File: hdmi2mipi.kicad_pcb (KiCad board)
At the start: 2 copper layers, 1 part

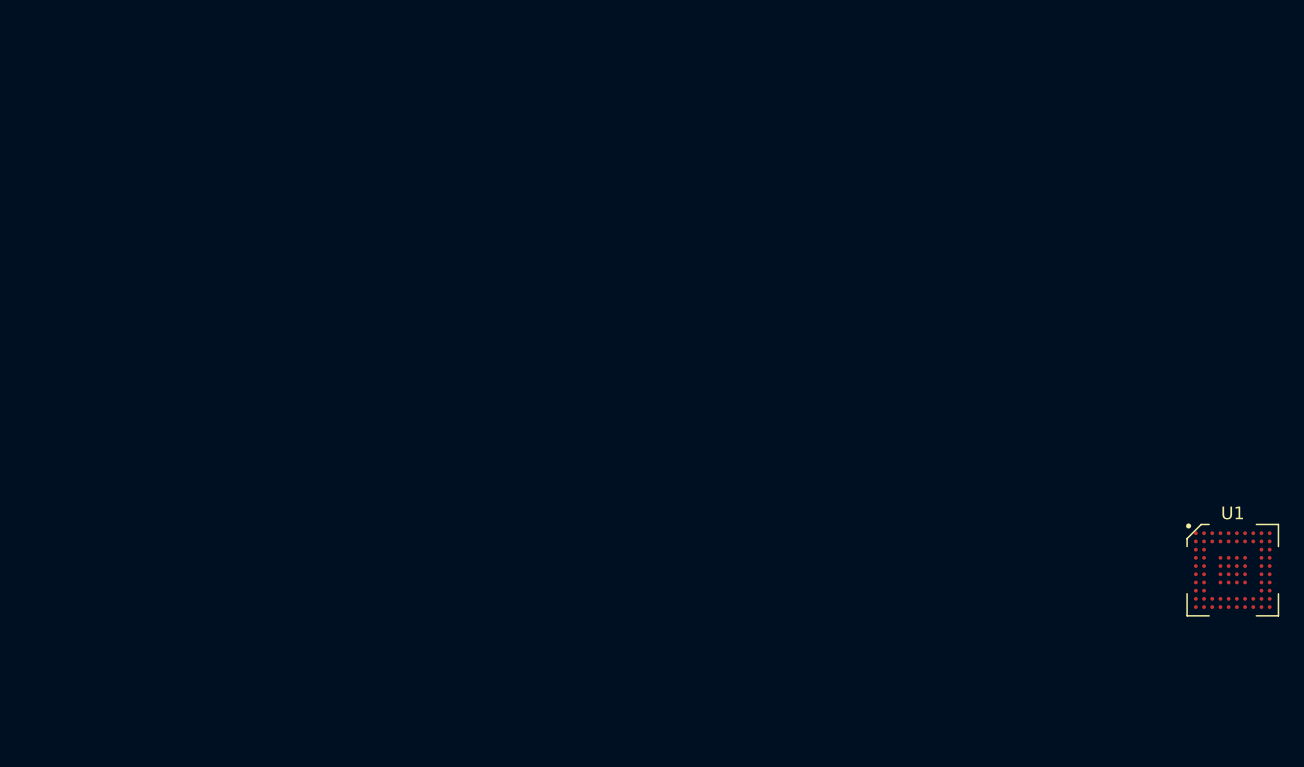
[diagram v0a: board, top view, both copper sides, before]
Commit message: Add RP2040, fix pinout, add transistors for controlling the 1.8v and 3.3v outputs on the MIPI connector
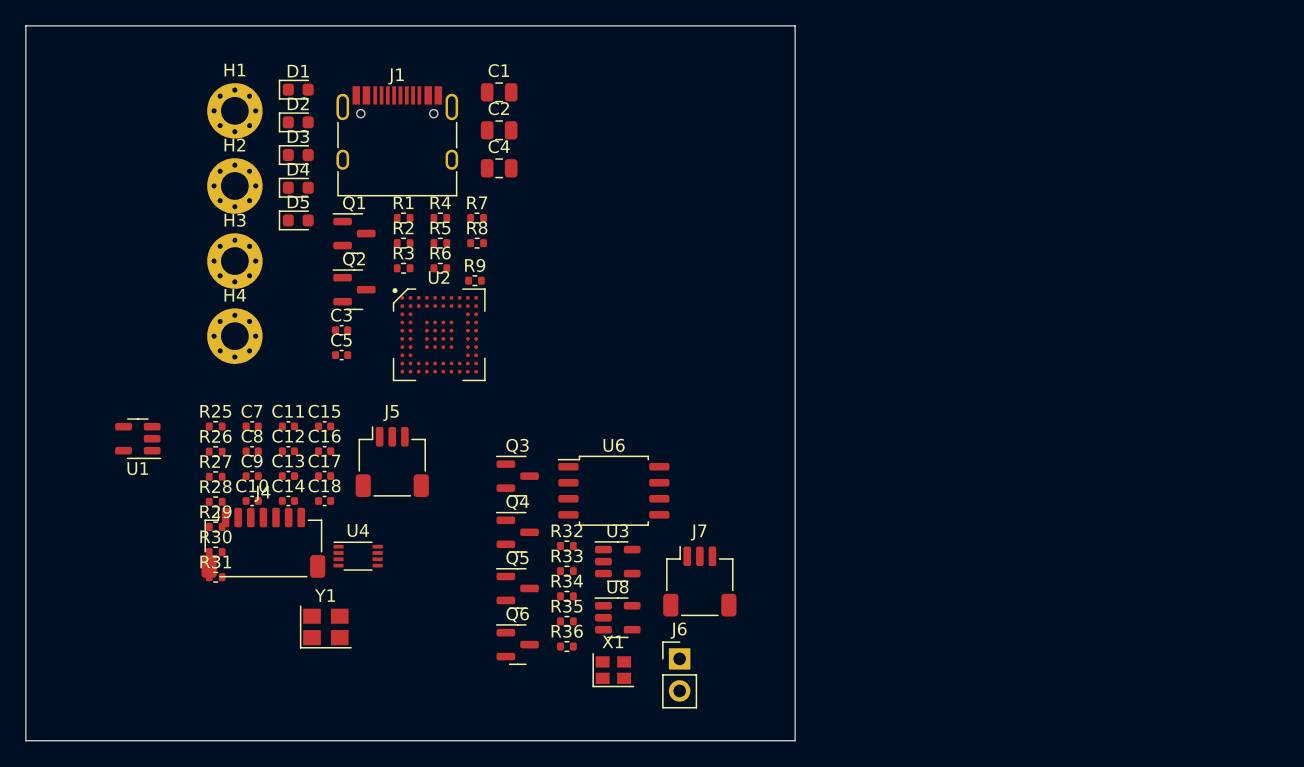
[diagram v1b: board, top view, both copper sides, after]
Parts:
- added C1: 22u, Capacitor_SMD:C_0805_2012Metric, F.Cu at (65.7, 24.8)
- added C10: 100n, Capacitor_SMD:C_0402_1005Metric, F.Cu at (46.1, 57.1)
- added C11: 1u, Capacitor_SMD:C_0402_1005Metric, F.Cu at (49.0, 51.2)
- added C12: 100n, Capacitor_SMD:C_0402_1005Metric, F.Cu at (49.0, 53.2)
- added C13: 100n, Capacitor_SMD:C_0402_1005Metric, F.Cu at (49.0, 55.2)
- added C14: 100n, Capacitor_SMD:C_0402_1005Metric, F.Cu at (49.0, 57.1)
- added C15: 100n, Capacitor_SMD:C_0402_1005Metric, F.Cu at (51.9, 51.2)
- added C16: 100n, Capacitor_SMD:C_0402_1005Metric, F.Cu at (51.9, 53.2)
- added C17: 22p, Capacitor_SMD:C_0402_1005Metric, F.Cu at (51.9, 55.2)
- added C18: 22p, Capacitor_SMD:C_0402_1005Metric, F.Cu at (51.9, 57.1)
- added C2: 22u, Capacitor_SMD:C_0805_2012Metric, F.Cu at (65.7, 27.8)
- added C3: 22p, Capacitor_SMD:C_0402_1005Metric, F.Cu at (53.2, 43.6)
- added C4: 22u, Capacitor_SMD:C_0805_2012Metric, F.Cu at (65.7, 30.8)
- added C5: 100n, Capacitor_SMD:C_0402_1005Metric, F.Cu at (53.2, 45.6)
- added C7: 100n, Capacitor_SMD:C_0402_1005Metric, F.Cu at (46.1, 51.2)
- added C8: 1u, Capacitor_SMD:C_0402_1005Metric, F.Cu at (46.1, 53.2)
- added C9: 100n, Capacitor_SMD:C_0402_1005Metric, F.Cu at (46.1, 55.2)
- added D1: LED, LED_SMD:LED_0603_1608Metric, F.Cu at (49.8, 24.6)
- added D2: LED, LED_SMD:LED_0603_1608Metric, F.Cu at (49.8, 27.1)
- added D3: LED, LED_SMD:LED_0603_1608Metric, F.Cu at (49.8, 29.7)
- added D4: LED, LED_SMD:LED_0603_1608Metric, F.Cu at (49.8, 32.3)
- added D5: LED, LED_SMD:LED_0603_1608Metric, F.Cu at (49.8, 34.9)
- added H1: MountingHole_Pad, MountingHole:MountingHole_2.2mm_M2_Pad_Via, F.Cu at (44.7, 26.2)
- added H2: MountingHole_Pad, MountingHole:MountingHole_2.2mm_M2_Pad_Via, F.Cu at (44.7, 32.2)
- added H3: MountingHole_Pad, MountingHole:MountingHole_2.2mm_M2_Pad_Via, F.Cu at (44.7, 38.1)
- added H4: MountingHole_Pad, MountingHole:MountingHole_2.2mm_M2_Pad_Via, F.Cu at (44.7, 44.1)
- added J1: USB_C_Receptacle_USB2.0, Connector_USB:USB_C_Receptacle_HRO_TYPE-C-31-M-12, F.Cu at (57.6, 29.1)
- added J4: TP, Connector_JST:JST_SH_SM07B-SRSS-TB_1x07-1MP_P1.00mm_Horizontal, F.Cu at (47.0, 60.5)
- added J5: SWD, Connector_JST:JST_SH_SM03B-SRSS-TB_1x03-1MP_P1.00mm_Horizontal, F.Cu at (57.2, 54.1)
- added J6: BOOT, Connector_PinHeader_2.54mm:PinHeader_1x02_P2.54mm_Vertical, F.Cu at (80.0, 69.7)
- added J7: SWD, Connector_JST:JST_SH_SM03B-SRSS-TB_1x03-1MP_P1.00mm_Horizontal, F.Cu at (81.6, 63.5)
- added Q1: BC846, Package_TO_SOT_SMD:SOT-23, F.Cu at (54.2, 36.0)
- added Q2: BC846, Package_TO_SOT_SMD:SOT-23, F.Cu at (54.2, 40.4)
- added Q3: BC846, Package_TO_SOT_SMD:SOT-23, F.Cu at (67.2, 55.2)
- added Q4: BC846, Package_TO_SOT_SMD:SOT-23, F.Cu at (67.2, 59.6)
- added Q5: BC846, Package_TO_SOT_SMD:SOT-23, F.Cu at (67.2, 64.1)
- added Q6: BC846, Package_TO_SOT_SMD:SOT-23, F.Cu at (67.2, 68.5)
- added R1: 1k, Resistor_SMD:R_0402_1005Metric, F.Cu at (58.1, 34.7)
- added R2: 1k, Resistor_SMD:R_0402_1005Metric, F.Cu at (58.1, 36.7)
- added R25: 1k, Resistor_SMD:R_0402_1005Metric, F.Cu at (43.2, 51.2)
- added R26: 27, Resistor_SMD:R_0402_1005Metric, F.Cu at (43.2, 53.2)
- added R27: 27, Resistor_SMD:R_0402_1005Metric, F.Cu at (43.2, 55.2)
- added R28: 1k, Resistor_SMD:R_0402_1005Metric, F.Cu at (43.2, 57.2)
- added R29: 100, Resistor_SMD:R_0402_1005Metric, F.Cu at (43.2, 59.2)
- added R3: 1k, Resistor_SMD:R_0402_1005Metric, F.Cu at (58.1, 38.7)
- added R30: 1k, Resistor_SMD:R_0402_1005Metric, F.Cu at (43.2, 61.2)
- added R31: 27, Resistor_SMD:R_0402_1005Metric, F.Cu at (43.2, 63.2)
- added R32: 27, Resistor_SMD:R_0402_1005Metric, F.Cu at (71.0, 60.7)
- added R33: 1k, Resistor_SMD:R_0402_1005Metric, F.Cu at (71.0, 62.7)
- added R34: 100, Resistor_SMD:R_0402_1005Metric, F.Cu at (71.0, 64.7)
- added R35: 100, Resistor_SMD:R_0402_1005Metric, F.Cu at (71.0, 66.7)
- added R36: 1k, Resistor_SMD:R_0402_1005Metric, F.Cu at (71.0, 68.7)
- added R4: 1k, Resistor_SMD:R_0402_1005Metric, F.Cu at (61.0, 34.7)
- added R5: 1k, Resistor_SMD:R_0402_1005Metric, F.Cu at (61.0, 36.7)
- added R6: 45.3k, Resistor_SMD:R_0402_1005Metric, F.Cu at (61.0, 38.7)
- added R7: 10k, Resistor_SMD:R_0402_1005Metric, F.Cu at (63.9, 34.7)
- added R8: 5.1k, Resistor_SMD:R_0402_1005Metric, F.Cu at (63.9, 36.7)
- added R9: 5.1k, Resistor_SMD:R_0402_1005Metric, F.Cu at (63.8, 39.7)
- added U2: ~, tc358840xbg:tc358840xbg, F.Cu at (60.9, 44.0)
- added U3: SY6280AAC, Package_TO_SOT_SMD:SOT-23-5, F.Cu at (75.1, 61.9)
- added U4: PCA9306DC, Package_SO:VSSOP-8_2.3x2mm_P0.5mm, F.Cu at (54.5, 61.5)
- added U6: W25Q16JVUXIQ, Package_SO:SOIC-8_5.23x5.23mm_P1.27mm, F.Cu at (74.8, 56.3)
- added U8: SY6280AAC, Package_TO_SOT_SMD:SOT-23-5, F.Cu at (75.1, 66.4)
- added X1: SG-210STF, Oscillator:Oscillator_SMD_SeikoEpson_SG210-4Pin_2.5x2.0mm, F.Cu at (74.7, 70.5)
- added Y1: 12MHz, Crystal:Crystal_SMD_3225-4Pin_3.2x2.5mm, F.Cu at (52.0, 67.1)
- U1: value ~ -> SY8079AAC; footprint tc358840xbg:tc358840xbg -> Package_TO_SOT_SMD:SOT-23-5
- moved U1 87.4 mm to (37.1, 52.2), turned to 180 degrees
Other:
- board outline added: 60.9 x 56.6 mm

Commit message: Most of schematic done, experimenting with component placement
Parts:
- added C19: 100n, Capacitor_SMD:C_0402_1005Metric, F.Cu at (15.5, -35.1)
- added C20: 22u, Capacitor_SMD:C_0805_2012Metric, F.Cu at (15.5, -33.3)
- added C21: 22p, Capacitor_SMD:C_0402_1005Metric, F.Cu at (24.4, -33.3)
- added C22: 22u, Capacitor_SMD:C_0805_2012Metric, F.Cu at (24.6, -39.1)
- added C23: 22u, Capacitor_SMD:C_0805_2012Metric, F.Cu at (24.6, -36.8)
- added C24: 100n, Capacitor_SMD:C_0402_1005Metric, F.Cu at (3.33, -35.1)
- added C25: 22u, Capacitor_SMD:C_0805_2012Metric, F.Cu at (3.56, -33.3)
- added C26: 22p, Capacitor_SMD:C_0402_1005Metric, F.Cu at (11.4, -33.5)
- added C27: 22u, Capacitor_SMD:C_0805_2012Metric, F.Cu at (11.7, -39.6)
- added C28: 22u, Capacitor_SMD:C_0805_2012Metric, F.Cu at (11.7, -37.3)
- added C29: 100n, Capacitor_SMD:C_0402_1005Metric, F.Cu at (42.2, -35.1)
- added C30: 22u, Capacitor_SMD:C_0805_2012Metric, F.Cu at (42.2, -33.3)
- added C31: 22p, Capacitor_SMD:C_0402_1005Metric, F.Cu at (50.0, -33.5)
- added C32: 22u, Capacitor_SMD:C_0805_2012Metric, F.Cu at (50.0, -40.1)
- added C33: 22u, Capacitor_SMD:C_0805_2012Metric, F.Cu at (49.9, -38.1)
- added C34: 100n, Capacitor_SMD:C_0402_1005Metric, F.Cu at (10.5, -12.5)
- added C35: 100n, Capacitor_SMD:C_0402_1005Metric, F.Cu at (10.5, -11.5)
- added C36: 100n, Capacitor_SMD:C_0402_1005Metric, F.Cu at (-0.97, -12.0)
- added C37: 22u, Capacitor_SMD:C_0805_2012Metric, F.Cu at (-7.62, -3.81)
- added C38: 100n, Capacitor_SMD:C_0402_1005Metric, F.Cu at (-0.34, -6.39)
- added C39: 1n, Capacitor_SMD:C_0402_1005Metric, F.Cu at (2.50, -2.50)
- added C40: 0.1u, Capacitor_SMD:C_0402_1005Metric, F.Cu at (2.00, -1.00)
- added C41: 0.1u, Capacitor_SMD:C_0402_1005Metric, F.Cu at (-0.50, -5.00)
- added C42: 5p, Capacitor_SMD:C_0402_1005Metric, F.Cu at (-0.50, -4.00)
- added C43: 1n, Capacitor_SMD:C_0402_1005Metric, F.Cu at (-0.50, -3.00)
- added C44: 1u, Capacitor_SMD:C_0402_1005Metric, F.Cu at (7.21, 5.92)
- added C45: 100n, Capacitor_SMD:C_0402_1005Metric, F.Cu at (6.18, 5.90)
- added C46: 100n, Capacitor_SMD:C_0402_1005Metric, F.Cu at (3.30, 1.98)
- added C47: 47u, Capacitor_SMD:C_0805_2012Metric, F.Cu at (2.80, 4.70)
- added C48: 47u, Capacitor_SMD:C_0805_2012Metric, F.Cu at (0.76, 2.78)
- added C49: 100n, Capacitor_SMD:C_0402_1005Metric, F.Cu at (10.2, 1.24)
- added C50: 100n, Capacitor_SMD:C_0402_1005Metric, F.Cu at (9.15, 1.23)
- added C51: 39n, Capacitor_SMD:C_0402_1005Metric, F.Cu at (8.16, 3.17)
- added C52: 39n, Capacitor_SMD:C_0402_1005Metric, F.Cu at (11.3, 3.16)
- added C6: ~, Capacitor_SMD:C_0402_1005Metric, F.Cu at (-32.4, -30.8)
- added J2: HDMI_A_1.4, Connector_HDMI:HDMI_A_Molex_208658-1001_Horizontal, F.Cu at (-18.0, -11.3)
- added J3: ~, fpc60:Hirose_FH52-60S-0.5SH_1x60-1MP_P0.50mm_Horizontal, F.Cu at (20.0, 0.00)
- added J8: AudioJack3, custom:Boom-audiojack-PJ-320B, F.Cu at (-13.8, 21.0)
- added L1: 2.2u, custom:Inductor_MSC20FC, F.Cu at (-11.4, -29.7)
- added L2: 2.2u, custom:Inductor_MSC20FC, F.Cu at (19.8, -30.2)
- added L3: 2.2u, custom:Inductor_MSC20FC, F.Cu at (7.87, -30.0)
- added L4: 2.2u, custom:Inductor_MSC20FC, F.Cu at (46.2, -30.5)
- added Q7: 2SC2712, Package_TO_SOT_SMD:SOT-23, F.Cu at (-3.38, -6.79)
- added R10: 2k, Resistor_SMD:R_0402_1005Metric, F.Cu at (0.04, -12.0)
- added R11: 48k, Resistor_SMD:R_0402_1005Metric, F.Cu at (-44.0, -28.8)
- added R12: 0, Resistor_SMD:R_0402_1005Metric, F.Cu at (1.00, -17.0)
- added R13: 1.5k, Resistor_SMD:R_0402_1005Metric, F.Cu at (2.03, -17.0)
- added R14: 4.7k, Resistor_SMD:R_0402_1005Metric, F.Cu at (-10.7, -22.4)
- added R15: 10k, Resistor_SMD:R_0402_1005Metric, F.Cu at (-7.62, -22.4)
- added R16: 33, Resistor_SMD:R_0402_1005Metric, F.Cu at (0.52, -14.5)
- added R17: 33, Resistor_SMD:R_0402_1005Metric, F.Cu at (0.50, -13.5)
- added R18: 1k, Resistor_SMD:R_0402_1005Metric, F.Cu at (-41.1, -30.8)
- added R19: 1k, Resistor_SMD:R_0402_1005Metric, F.Cu at (-4.83, -22.4)
- added R20: 4.7k, Resistor_SMD:R_0402_1005Metric, F.Cu at (-1.00, -17.0)
- added R21: 4.7k, Resistor_SMD:R_0402_1005Metric, F.Cu at (0.00, -17.0)
- added R22: 100k, Resistor_SMD:R_0402_1005Metric, F.Cu at (-2.00, -17.0)
- added R23: 4.7k, Resistor_SMD:R_0402_1005Metric, F.Cu at (-6.77, -0.25)
- added R24: 4.7k, Resistor_SMD:R_0402_1005Metric, F.Cu at (-41.1, -18.9)
- added R37: 33, Resistor_SMD:R_0402_1005Metric, F.Cu at (7.29, -2.79)
- added R38: 10k, Resistor_SMD:R_0402_1005Metric, F.Cu at (-38.1, -20.8)
- added R39: 10k, Resistor_SMD:R_0402_1005Metric, F.Cu at (12.4, 2.79)
- added R40: 10k, Resistor_SMD:R_0402_1005Metric, F.Cu at (-38.1, -16.9)
- added R41: 4.7k, Resistor_SMD:R_0402_1005Metric, F.Cu at (15.2, 5.08)
- added R42: 10k, Resistor_SMD:R_0402_1005Metric, F.Cu at (9.40, 6.60)
- added R43: 4.7k, Resistor_SMD:R_0402_1005Metric, F.Cu at (14.7, 6.86)
- added R44: 10k, Resistor_SMD:R_0402_1005Metric, F.Cu at (13.0, 12.2)
- added R45: 4.7k, Resistor_SMD:R_0402_1005Metric, F.Cu at (15.5, 10.4)
- added R46: 10k, Resistor_SMD:R_0402_1005Metric, F.Cu at (7.87, 12.2)
- added R47: 4.7k, Resistor_SMD:R_0402_1005Metric, F.Cu at (9.91, 12.2)
- added R48: 1k, Resistor_SMD:R_0402_1005Metric, F.Cu at (1.50, -2.50)
- added R49: 1.5k, Resistor_SMD:R_0402_1005Metric, F.Cu at (-0.50, -2.00)
- added R50: 10k, Resistor_SMD:R_0402_1005Metric, F.Cu at (-0.89, 0.31)
- added R51: 10k, Resistor_SMD:R_0402_1005Metric, F.Cu at (24.4, -34.3)
- added R52: 10k, Resistor_SMD:R_0402_1005Metric, F.Cu at (24.4, -32.3)
- added R53: 10k, Resistor_SMD:R_0402_1005Metric, F.Cu at (11.4, -34.5)
- added R54: 8.2k, Resistor_SMD:R_0402_1005Metric, F.Cu at (11.4, -32.5)
- added R55: 10k, Resistor_SMD:R_0402_1005Metric, F.Cu at (6.60, -37.1)
- added R56: 10k, Resistor_SMD:R_0402_1005Metric, F.Cu at (18.8, -37.1)
- added R57: 10k, Resistor_SMD:R_0402_1005Metric, F.Cu at (45.0, -37.8)
- added R58: 10k, Resistor_SMD:R_0402_1005Metric, F.Cu at (50.0, -34.5)
- added R59: 20k, Resistor_SMD:R_0402_1005Metric, F.Cu at (50.0, -32.5)
- added R60: 1k, Resistor_SMD:R_0402_1005Metric, F.Cu at (-2.29, -4.06)
- added R61: 330, Resistor_SMD:R_0402_1005Metric, F.Cu at (10.2, 3.15)
- added R62: 330, Resistor_SMD:R_0402_1005Metric, F.Cu at (9.17, 3.15)
- added U10: SY8079AAC, Package_TO_SOT_SMD:SOT-23-5, F.Cu at (7.87, -33.5)
- added U11: SY8079AAC, Package_TO_SOT_SMD:SOT-23-5, F.Cu at (46.3, -34.0)
- added U5: W25Q16JVUXIQ, custom:PSON50P300X200X60-9N, F.Cu at (1.24, 15.5)
- added U7: RP2040, custom:QFN40P700X700X90-57N, F.Cu at (-8.44, 6.98)
- added U9: SY8079AAC, Package_TO_SOT_SMD:SOT-23-5, F.Cu at (20.1, -33.8)
- J5: value SWD -> QWIIC; footprint Connector_JST:JST_SH_SM03B-SRSS-TB_1x03-1MP_P1.00mm_Horizontal -> Connector_JST:JST_SH_SM04B-SRSS-TB_1x04-1MP_P1.00mm_Horizontal
- R25, R28: value 1k -> 4.7k
- R26, R27: value 27 -> 4.7k
- R29: value 100 -> 4.7k
- U8: value SY6280AAC -> MS4344; footprint Package_TO_SOT_SMD:SOT-23-5 -> custom:SOP50P490X110-10N
- moved R26 117.0 mm to (-38.1, -30.8)
- moved R27 117.0 mm to (-38.1, -28.8)
- moved R28 117.0 mm to (-38.1, -26.8)
- moved R29 117.0 mm to (-38.1, -24.8)
- moved J6 115.6 mm to (-21.7, 14.7)
- moved R25 108.4 mm to (-41.1, -16.9)
- moved R36 108.3 mm to (-13.3, 0.70), turned to -90 degrees
- moved C5 105.6 mm to (-15.2, -34.8)
- moved R33 103.9 mm to (-13.8, 2.73), turned to 180 degrees
- moved C4 103.1 mm to (-15.5, -32.8)
- moved C11 102.0 mm to (-47.3, 17.8)
- moved C8 101.9 mm to (-50.2, 19.8)
- moved C13 101.4 mm to (-46.8, 21.7)
- moved C10 101.4 mm to (-49.6, 23.7)
- moved R4 101.1 mm to (-34.3, 1.27)
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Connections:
- net MC_VSUPPLY_11 renamed +1V1
- net MC_VSUPPLY_12 renamed +1V2
- net VIN renamed VBUS
- J4 pad 5: /TP_VSUPPLY_18 -> +1V8
- J4 pad 6: /TP_VSUPPLY_33 -> 3V3_HDMI
- J5 pad 1: Net-(J5-Pin_1) -> GND
- J5 pad 2: GND -> +3V3
- J5 pad MP: (no net) -> GND
- Q3 pad 1: Net-(Q3-B) -> 3V3_S2
- Q4 pad 1: Net-(Q4-B) -> 3V3_S1
- Q5 pad 1: Net-(Q5-B) -> 1V8_S2
- Q6 pad 1: Net-(Q6-B) -> 1V8_S1
- R1 pad 1: unconnected-(R1-Pad1) -> Net-(U7-GPIO11)
- R2 pad 1: unconnected-(R2-Pad1) -> Net-(U7-GPIO12)
- R25 pad 1: /Microcontroller/RP_QSPI_CSN -> +1V8
- R25 pad 2: /Microcontroller/RP_BTN -> Net-(J4-Pin_4)
- R26 pad 1: /Microcontroller/USB_DN -> +3V3
- R26 pad 2: Net-(U5-USB_DM) -> Net-(J5-Pin_3)
- R27 pad 1: Net-(U5-USB_DP) -> 3V3_HDMI
- R27 pad 2: /Microcontroller/USB_DP -> Net-(U2-I2C_SCL)
- R28 pad 1: Net-(U5-RUN) -> +3V3
- R28 pad 2: +3V3 -> Net-(J5-Pin_4)
- R29 pad 1: Net-(J5-Pin_1) -> 3V3_HDMI
- R29 pad 2: Net-(U5-SWCLK) -> Net-(U2-I2C_SDA)
- R3 pad 1: unconnected-(R3-Pad1) -> Net-(U7-GPIO13)
- R4 pad 1: unconnected-(R4-Pad1) -> Net-(U7-GPIO14)
- R5 pad 1: unconnected-(R5-Pad1) -> Net-(U7-GPIO10)
- U2 pad A5: Net-(J3-Pin_3) -> /DSI1_D3_P
- U2 pad A6: Net-(J3-Pin_6) -> /DSI1_D2_P
- U2 pad A7: Net-(J3-Pin_9) -> /DSI1_C_P
- U2 pad A8: Net-(J3-Pin_12) -> /DSI1_D1_P
- U2 pad A9: Net-(J3-Pin_15) -> /DSI1_D0_P
- U2 pad B1: VDD33_HDMI -> 3V3_HDMI
- U2 pad B5: Net-(J3-Pin_2) -> /DSI1_D3_N
- U2 pad B6: Net-(J3-Pin_5) -> /DSI1_D2_N
- U2 pad B7: Net-(J3-Pin_8) -> /DSI1_C_N
- U2 pad B8: Net-(J3-Pin_11) -> /DSI1_D1_N
- U2 pad B9: Net-(J3-Pin_14) -> /DSI1_D0_N
- U2 pad C1: Net-(J2-CK+) -> /HDMI_C_P
- U2 pad C2: Net-(J2-CK-) -> /HDMI_C_N
- U2 pad D1: Net-(J2-D0+) -> /HDMI_0_P
- U2 pad D10: Net-(J3-Pin_18) -> /DSI0_D3_P
- U2 pad D2: Net-(J2-D0-) -> /HDMI_0_N
- U2 pad D9: Net-(J3-Pin_17) -> /DSI0_D3_N
- U2 pad E1: Net-(J2-D1+) -> /HDMI_1_P
- U2 pad E10: Net-(J3-Pin_21) -> /DSI0_D2_P
- U2 pad E2: Net-(J2-D1-) -> /HDMI_1_N
- U2 pad E9: Net-(J3-Pin_20) -> /DSI0_D2_N
- U2 pad F1: Net-(J2-D2+) -> /HDMI_2_P
- U2 pad F10: Net-(J3-Pin_24) -> /DSI0_C_P
- U2 pad F2: Net-(J2-D2-) -> /HDMI_2_N
- U2 pad F9: Net-(J3-Pin_23) -> /DSI0_C_N
- U2 pad G1: VDD33_HDMI -> 3V3_HDMI
- U2 pad G10: Net-(J3-Pin_27) -> /DSI0_D1_P
- U2 pad G9: Net-(J3-Pin_26) -> /DSI0_D1_N
- U2 pad H10: Net-(J3-Pin_30) -> /DSI0_D0_P
- U2 pad H2: VDD33_HDMI -> 3V3_HDMI
- U2 pad H9: Net-(J3-Pin_29) -> /DSI0_D0_N
- U2 pad J1: unconnected-(U2-BIASDA-PadJ1) -> Net-(U2-BIASDA)
- U2 pad J2: unconnected-(U2-DAOUT-PadJ2) -> Net-(U2-DAOUT)
- U2 pad J3: MC_I2C_INT -> Net-(U2-INT)
- U2 pad J4: unconnected-(U2-A_OSCK-PadJ4) -> Net-(U2-A_OSCK)
- U2 pad J7: VDD33_HDMI -> 3V3_HDMI
- U2 pad J9: unconnected-(U2-A_SD0-PadJ9) -> Net-(U2-A_SD0)
- U2 pad K1: unconnected-(U2-PCKIN-PadK1) -> Net-(U2-PCKIN)
- U2 pad K2: unconnected-(U2-PFIL-PadK2) -> Net-(U2-PFIL)
- U2 pad K5: unconnected-(U2-A_WFS-PadK5) -> Net-(U2-A_WFS)
- U2 pad K7: unconnected-(U2-A_SCK-PadK7) -> Net-(U2-A_SCK)
- U2 pad K8: MC_I2C_RESET -> Net-(U2-~{RESET})
- U3 pad 1: VDD33_HDMI -> 3V3_HDMI
- U4 pad 2: /TP_VSUPPLY_18 -> +1V8
- U8 pad 1: Net-(J3-Pin_36) -> Net-(U2-A_SD0)
- U8 pad 2: GND -> Net-(U2-A_SCK)
- U8 pad 3: Net-(U8-SET) -> Net-(U2-A_WFS)
- U8 pad 4: Net-(U7-GPIO3) -> Net-(U2-A_OSCK)
- U8 pad 5: +3V3 -> Net-(U8-VQ)
- X1 pad 1: VDD33_HDMI -> 3V3_HDMI
- X1 pad 4: VDD33_HDMI -> 3V3_HDMI
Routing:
- net GND: track 0.00 -> 157.8 mm, vias 0 -> 45
- net /AUDIO_R: track 0.00 -> 42.0 mm, vias 0 -> 2
- net /AUDIO_L: track 0.00 -> 30.5 mm, vias 0 -> 2
- net +1V1: track 0.00 -> 24.3 mm, vias 0 -> 4
- net 3V3_HDMI: track 0.00 -> 23.5 mm, vias 0 -> 5
- net /DSI0_D1_N: track 0.00 -> 22.8 mm
- net /DSI1_D3_N: track 0.00 -> 22.2 mm
- net /DSI1_D3_P: track 0.00 -> 22.2 mm
- net /DSI1_D2_N: track 0.00 -> 22.0 mm
- net /DSI1_C_N: track 0.00 -> 21.9 mm
- net /DSI1_D1_N: track 0.00 -> 21.9 mm
- net /DSI1_D2_P: track 0.00 -> 21.9 mm
- net /DSI1_C_P: track 0.00 -> 21.9 mm
- net /DSI1_D1_P: track 0.00 -> 21.9 mm
- net /DSI0_D1_P: track 0.00 -> 21.8 mm
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- added copper zone on In2.Cu, net +1V1
- added copper zone on In2.Cu, net +1V2
- added copper zone on In2.Cu, net +3V3
- added copper zone on F.Cu, net GND
- added copper zone on In1.Cu, net GND
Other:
- board size 60.9 x 56.6 mm -> 50 x 50 mm
- copper layers 2 -> 4

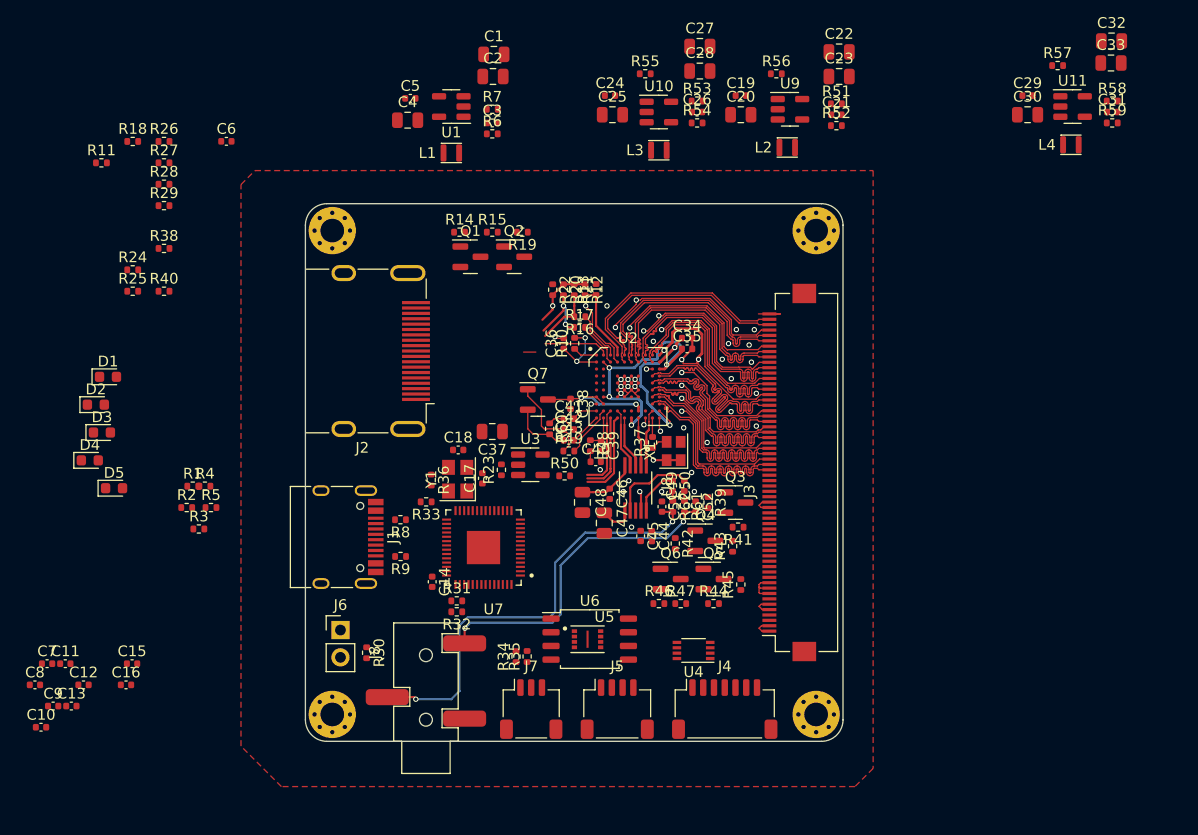
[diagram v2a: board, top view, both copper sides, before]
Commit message: Board to 7cm+-
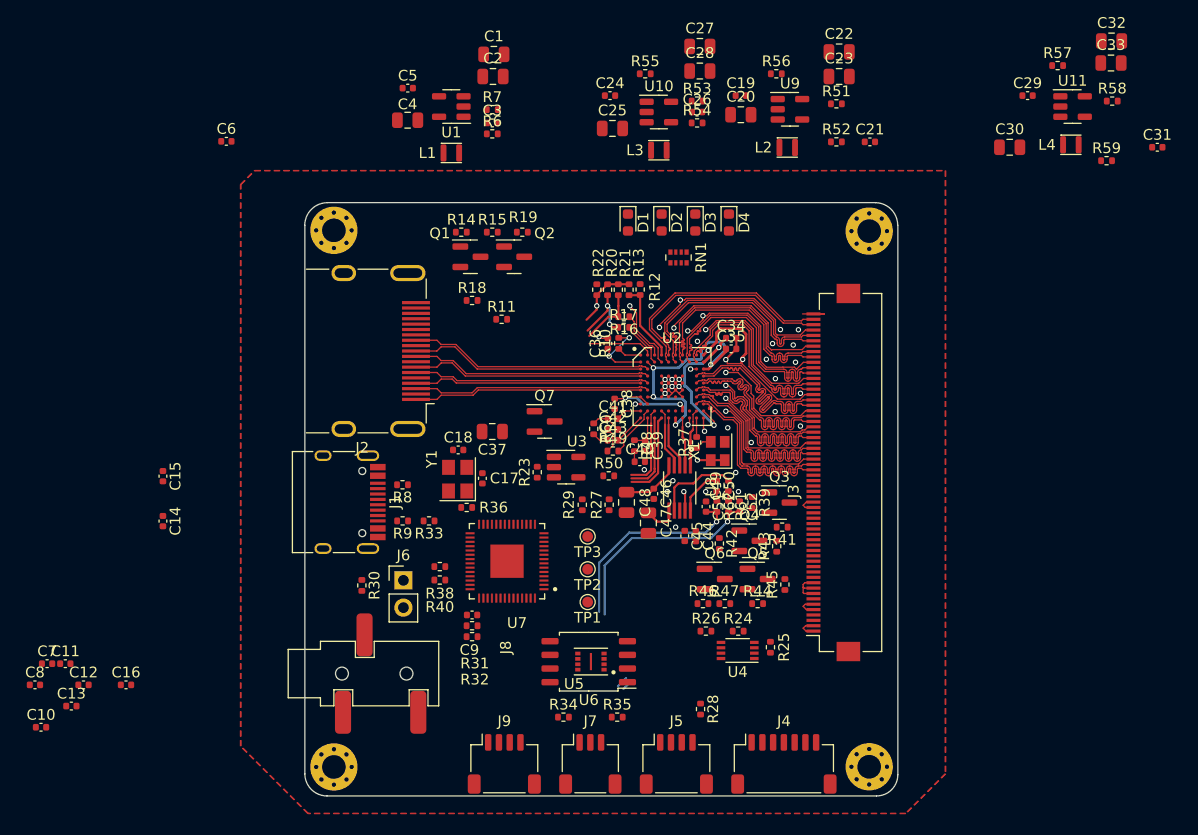
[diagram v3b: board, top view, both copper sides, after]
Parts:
- removed D5: LED, LED_SMD:LED_0603_1608Metric
- removed R1, R2, R3, R4, R5: 1k, Resistor_SMD:R_0402_1005Metric
- added J9: QWIIC, Connector_JST:JST_SH_SM04B-SRSS-TB_1x04-1MP_P1.00mm_Horizontal, F.Cu at (-6.50, 27.1)
- added RN1: 1K, Resistor_SMD:R_Array_Convex_4x0402, F.Cu at (9.70, -20.0)
- added TP1: TestPoint, TestPoint:TestPoint_Pad_D1.0mm, F.Cu at (1.25, 12.1)
- added TP2: TestPoint, TestPoint:TestPoint_Pad_D1.0mm, F.Cu at (1.25, 9.00)
- added TP3: TestPoint, TestPoint:TestPoint_Pad_D1.0mm, F.Cu at (1.25, 5.95)
- moved R28 69.8 mm to (11.8, 22.0), turned to -90 degrees
- moved R26 67.9 mm to (12.2, 14.8)
- moved R25 67.9 mm to (18.2, 16.2), turned to 90 degrees
- moved R24 65.6 mm to (15.2, 14.8)
- moved D4 63.4 mm to (14.4, -23.2), turned to -90 degrees
- moved D3 58.5 mm to (11.3, -23.2), turned to -90 degrees
- moved D2 55.3 mm to (8.13, -23.2), turned to -90 degrees
- moved R27 52.2 mm to (3.25, 3.00), turned to 90 degrees
- moved D1 50.4 mm to (5.00, -23.2), turned to -90 degrees
- moved R29 47.8 mm to (0.75, 3.00), turned to -90 degrees
- moved R11 40.0 mm to (-6.75, -14.2)
- moved C9 39.9 mm to (-9.50, 13.2), turned to 180 degrees
- moved R38 39.2 mm to (-12.5, 8.75), turned to 180 degrees
- moved R40 37.1 mm to (-12.5, 10.0), turned to 180 degrees
- moved R18 34.9 mm to (-9.50, -16.0)
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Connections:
- U7 pad 13: Net-(U7-GPIO10) -> unconnected-(U7-GPIO10-Pad13)
- U7 pad 6: unconnected-(U7-GPIO4-Pad6) -> Net-(U7-GPIO4)
- U7 pad 7: unconnected-(U7-GPIO5-Pad7) -> Net-(U7-GPIO5)
- U7 pad 8: unconnected-(U7-GPIO6-Pad8) -> Net-(U7-GPIO6)
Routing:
- net /HDMI_C_N: track 0.00 -> 22.7 mm
- net /HDMI_0_N: track 0.00 -> 22.4 mm
- net /HDMI_2_N: track 0.00 -> 22.0 mm
- net /HDMI_1_N: track 0.00 -> 22.0 mm
- net /AUDIO_R: track 42.0 -> 20.1 mm, vias 2 -> 1
- net /HDMI_0_P: track 0.00 -> 21.6 mm
- net /HDMI_2_P: track 0.00 -> 21.3 mm
- net /HDMI_1_P: track 0.00 -> 21.2 mm
- net /HDMI_C_P: track 1.15 -> 21.9 mm
- net /AUDIO_L: track 30.5 -> 20.8 mm, vias 2 -> 1
- net Net-(Q7-B): track 8.55 -> 2.40 mm
- net Net-(Q7-E): track 5.56 -> 1.54 mm
- net 3V3_HDMI: track 23.5 -> 21.8 mm
- added copper zone on F.Cu, net 3V3_HDMI
- added copper zone on In1.Cu, net 3V3_HDMI
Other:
- board size 50 x 50 mm -> 55.2 x 55.2 mm
